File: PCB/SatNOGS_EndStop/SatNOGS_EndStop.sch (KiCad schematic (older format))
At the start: 6 parts, among them P1 CONN_01X03, U1 TCST2103

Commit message: Delete gerber files, update endstop and encoder PCB. Delete gerber files according to repo policy. Update the PCBs with 3d models and small fixes.
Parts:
- U1: footprint library:TCST2103 -> satnogs:TCST2103
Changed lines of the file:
@@
 LIBS:valves
 LIBS:satnogs
+LIBS:SatNOGS_EndStop-cache
 EELAYER 25 0
 EELAYER END
@@
 F 0 "U1" H 4950 2650 60  0000 C BNN
 F 1 "TCST2103" H 4700 3250 60  0000 C TNN
-F 2 "library:TCST2103" H 4700 2950 60  0001 C CNN
+F 2 "satnogs:TCST2103" H 4700 2950 60  0001 C CNN
 F 3 "" H 4700 2950 60  0000 C CNN
 	1    4700 2950

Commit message: Update 3d model of PCB and BOM.
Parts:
- D1: Distributor (none) -> SparkFun COM-09650; Manufacturer (none) -> -; Notes (none) -> -; Package (none) -> Green 3mm pitch 2.54; Price (none) -> 0.33€
- P1: Distributor (none) -> SparkFun PRT-00553; Manufacturer (none) -> -; Notes (none) -> -; Package (none) -> 1x40 pin right-angle pitch 2.54; Price (none) -> 1.85€
- R1: Distributor (none) -> Mouser 71-CRCW0805180RJNEA; Manufacturer (none) -> CRCW0805180RJNEA; Notes (none) -> 1/8W 5%; Package (none) -> 0805; Price (none) -> 0.091 €
- R2: Distributor (none) -> Mouser 71-CRCW0805J-1.5K-E3; Manufacturer (none) -> CRCW08051K50JNEA; Notes (none) -> 1/8W 5%; Package (none) -> 0805; Price (none) -> 0.091€
- R3: Distributor (none) -> Mouser 71-CRCW08051K00JNEB; Manufacturer (none) -> CRCW08051K00JNEB; Notes (none) -> 1/8W 5%; Package (none) -> 0805; Price (none) -> 0.091€
- U1: Distributor (none) -> Mouser 782-TCST2103; Manufacturer (none) -> TCST2103; Notes (none) -> -; Package (none) -> -; Price (none) -> 1.59€
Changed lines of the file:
@@
 F 1 "TCST2103" H 4700 3250 60  0000 C TNN
 F 2 "satnogs:TCST2103" H 4700 2950 60  0001 C CNN
-F 3 "" H 4700 2950 60  0000 C CNN
+F 3 "http://www.mouser.com/ds/2/427/tcst2103-279826.pdf" H 4700 2950 60  0001 C CNN
+F 4 "Mouser 782-TCST2103 " H 4700 2950 60  0001 C CNN "Distributor"
+F 5 "TCST2103" H 4700 2950 60  0001 C CNN "Manufacturer"
+F 6 "-" H 4700 2950 60  0001 C CNN "Package"
+F 7 "-" H 4700 2950 60  0001 C CNN "Notes"
+F 8 "1.59€" H 4700 2950 60  0001 C CNN "Price"
 	1    4700 2950
 	1    0    0    -1
@@
 F 1 "180" V 4100 2450 50  0000 C CNN
 F 2 "Resistors_SMD:R_0805_HandSoldering" V 4030 2450 30  0001 C CNN
-F 3 "" H 4100 2450 30  0000 C CNN
+F 3 "http://www.mouser.com/ds/2/427/dcrcwe3-109170.pdf" H 4100 2450 30  0001 C CNN
+F 4 "Mouser 71-CRCW0805180RJNEA " V 4100 2450 60  0001 C CNN "Distributor"
+F 5 "CRCW0805180RJNEA" V 4100 2450 60  0001 C CNN "Manufacturer"
+F 6 "0805" V 4100 2450 60  0001 C CNN "Package"
+F 7 "1/8W 5%" V 4100 2450 60  0001 C CNN "Notes"
+F 8 "0.091 €" V 4100 2450 60  0001 C CNN "Price"
 	1    4100 2450
 	1    0    0    -1
@@
 F 1 "1k5" V 5650 2450 50  0000 C CNN
 F 2 "Resistors_SMD:R_0805_HandSoldering" V 5580 2450 30  0001 C CNN
-F 3 "" H 5650 2450 30  0000 C CNN
+F 3 "http://www.mouser.com/ds/2/427/dcrcwe3-109170.pdf" H 5650 2450 30  0001 C CNN
+F 4 "Mouser 71-CRCW0805J-1.5K-E3" V 5650 2450 60  0001 C CNN "Distributor"
+F 5 "CRCW08051K50JNEA" V 5650 2450 60  0001 C CNN "Manufacturer"
+F 6 "0805" V 5650 2450 60  0001 C CNN "Package"
+F 7 "1/8W 5%" V 5650 2450 60  0001 C CNN "Notes"
+F 8 "0.091€" V 5650 2450 60  0001 C CNN "Price"
 	1    5650 2450
 	1    0    0    -1
@@
 F 1 "1k" V 5650 3800 50  0000 C CNN
 F 2 "Resistors_SMD:R_0805_HandSoldering" V 5580 3800 30  0001 C CNN
-F 3 "" H 5650 3800 30  0000 C CNN
+F 3 "http://www.mouser.com/ds/2/427/dcrcwe3-109170.pdf" H 5650 3800 30  0001 C CNN
+F 4 "Mouser 71-CRCW08051K00JNEB " V 5650 3800 60  0001 C CNN "Distributor"
+F 5 "CRCW08051K00JNEB" V 5650 3800 60  0001 C CNN "Manufacturer"
+F 6 "0805" V 5650 3800 60  0001 C CNN "Package"
+F 7 "1/8W 5%" V 5650 3800 60  0001 C CNN "Notes"
+F 8 "0.091€" V 5650 3800 60  0001 C CNN "Price"
 	1    5650 3800
 	1    0    0    -1
@@
 F 1 "LED" H 5650 3250 50  0000 C CNN
 F 2 "LEDs:LED-3MM" H 5650 3350 60  0001 C CNN
-F 3 "" H 5650 3350 60  0000 C CNN
+F 3 "https://www.sparkfun.com/datasheets/Components/LED/YSL-R341K3D-D2.pdf" H 5650 3350 60  0001 C CNN
+F 4 "SparkFun COM-09650" H 5650 3350 60  0001 C CNN "Distributor"
+F 5 "-" H 5650 3350 60  0001 C CNN "Manufacturer"
+F 6 "Green 3mm pitch 2.54" H 5650 3350 60  0001 C CNN "Package"
+F 7 "-" H 5650 3350 60  0001 C CNN "Notes"
+F 8 "0.33€" H 5650 3350 60  0001 C CNN "Price"
 	1    5650 3350
 	0    -1   -1   0
@@
 F 1 "CONN_01X03" V 7325 3000 50  0000 C CNN
 F 2 "Pin_Headers:Pin_Header_Angled_1x03" H 7225 3000 60  0001 C CNN
-F 3 "" H 7225 3000 60  0000 C CNN
+F 3 "-" H 7225 3000 60  0001 C CNN
+F 4 "SparkFun PRT-00553" H 7225 3000 60  0001 C CNN "Distributor"
+F 5 "-" H 7225 3000 60  0001 C CNN "Manufacturer"
+F 6 "1x40 pin right-angle pitch 2.54" H 7225 3000 60  0001 C CNN "Package"
+F 7 "-" H 7225 3000 60  0001 C CNN "Notes"
+F 8 "1.85€" H 7225 3000 60  0001 C CNN "Price"
 	1    7225 3000
 	1    0    0    -1

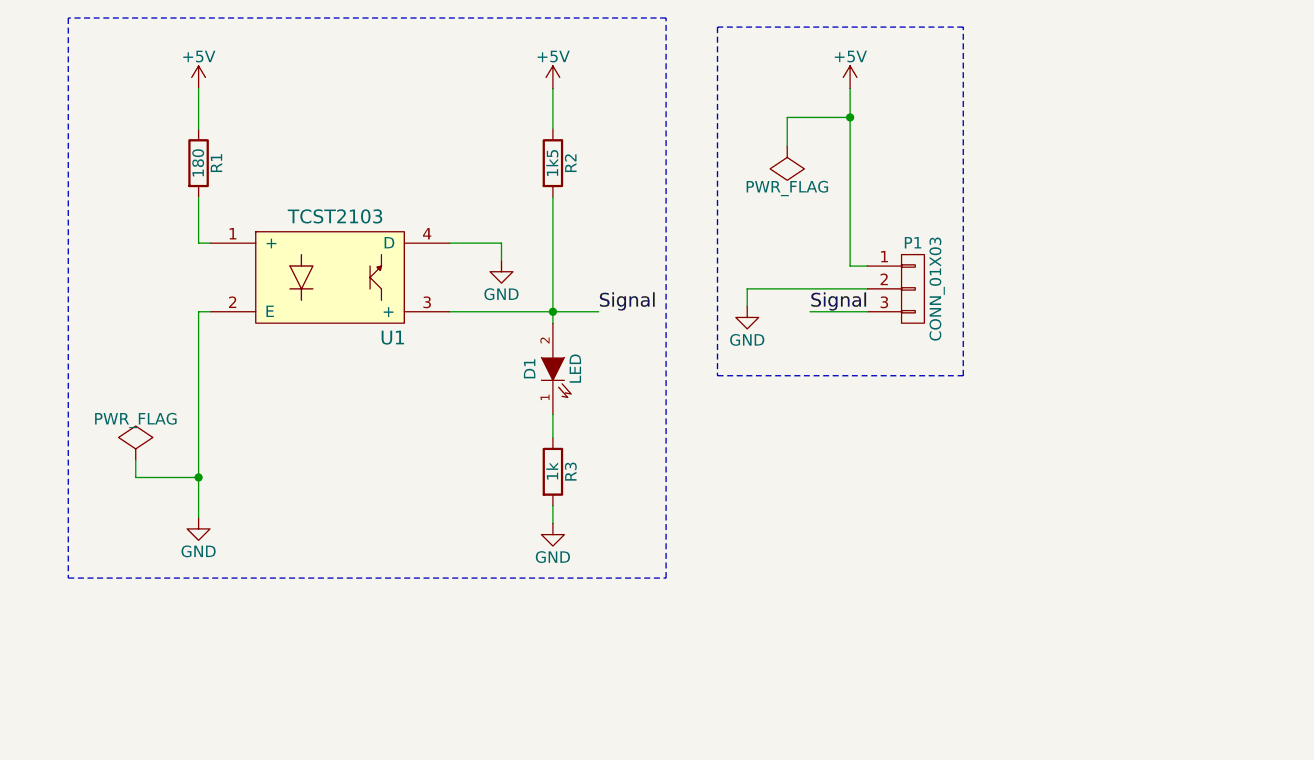
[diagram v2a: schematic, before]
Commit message: Add reverse current protection to end-stop PCB.
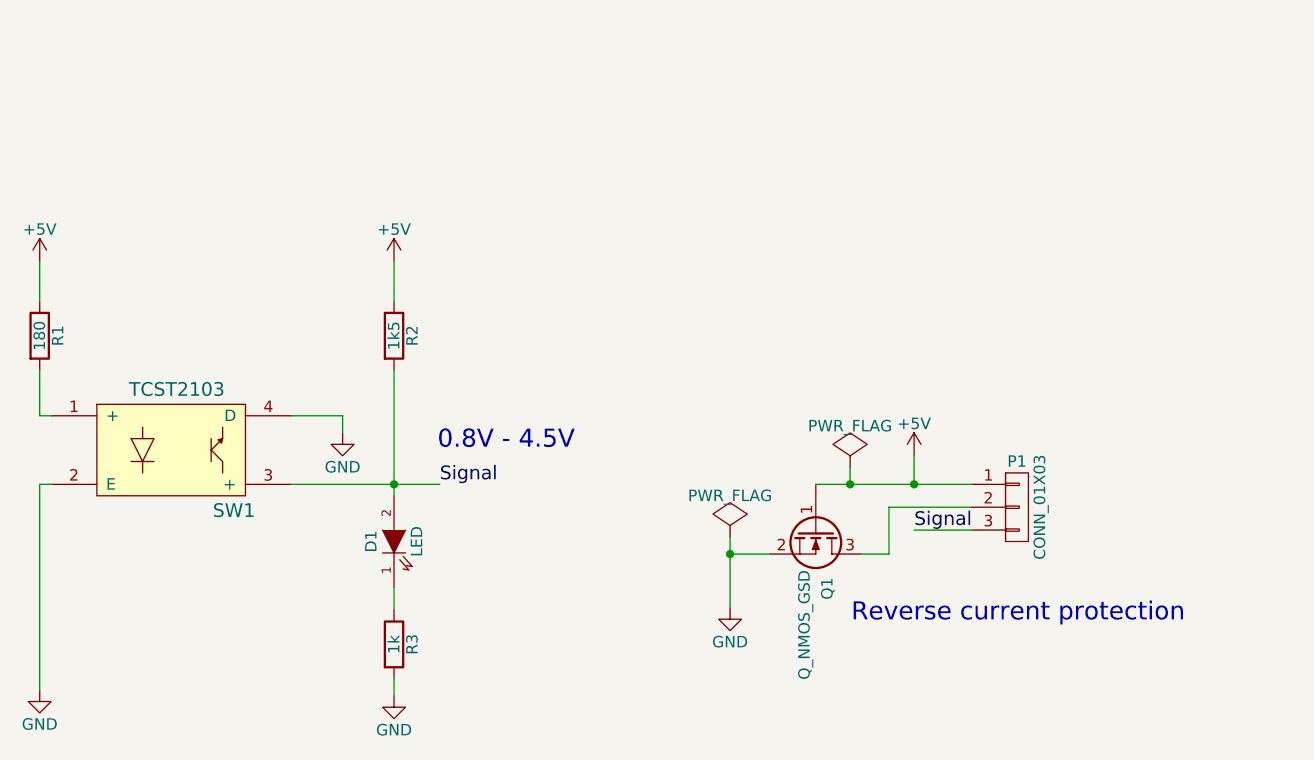
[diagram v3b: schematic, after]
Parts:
- added Q1: Q_NMOS_GSD, TO_SOT_Packages_SMD:SOT-23_Handsoldering, symbol Q_NMOS_GSD
- renumbered U1 to SW1
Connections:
- net +5V: now also Q1.1 (G)
- net GND: now also Q1.2 (S); no longer P1.2 (P2)
- new net: P1.2 (P2), Q1.3 (D)
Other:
- note added: "0.8V - 4.5V"
- note added: "Reverse current protection"
- moved on the sheet: D1, P1, R1, R2, R3, SW1
